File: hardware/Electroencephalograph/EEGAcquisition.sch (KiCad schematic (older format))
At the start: 59 parts, among them U1 ADS1298IPAG, U2 OPA330xxD

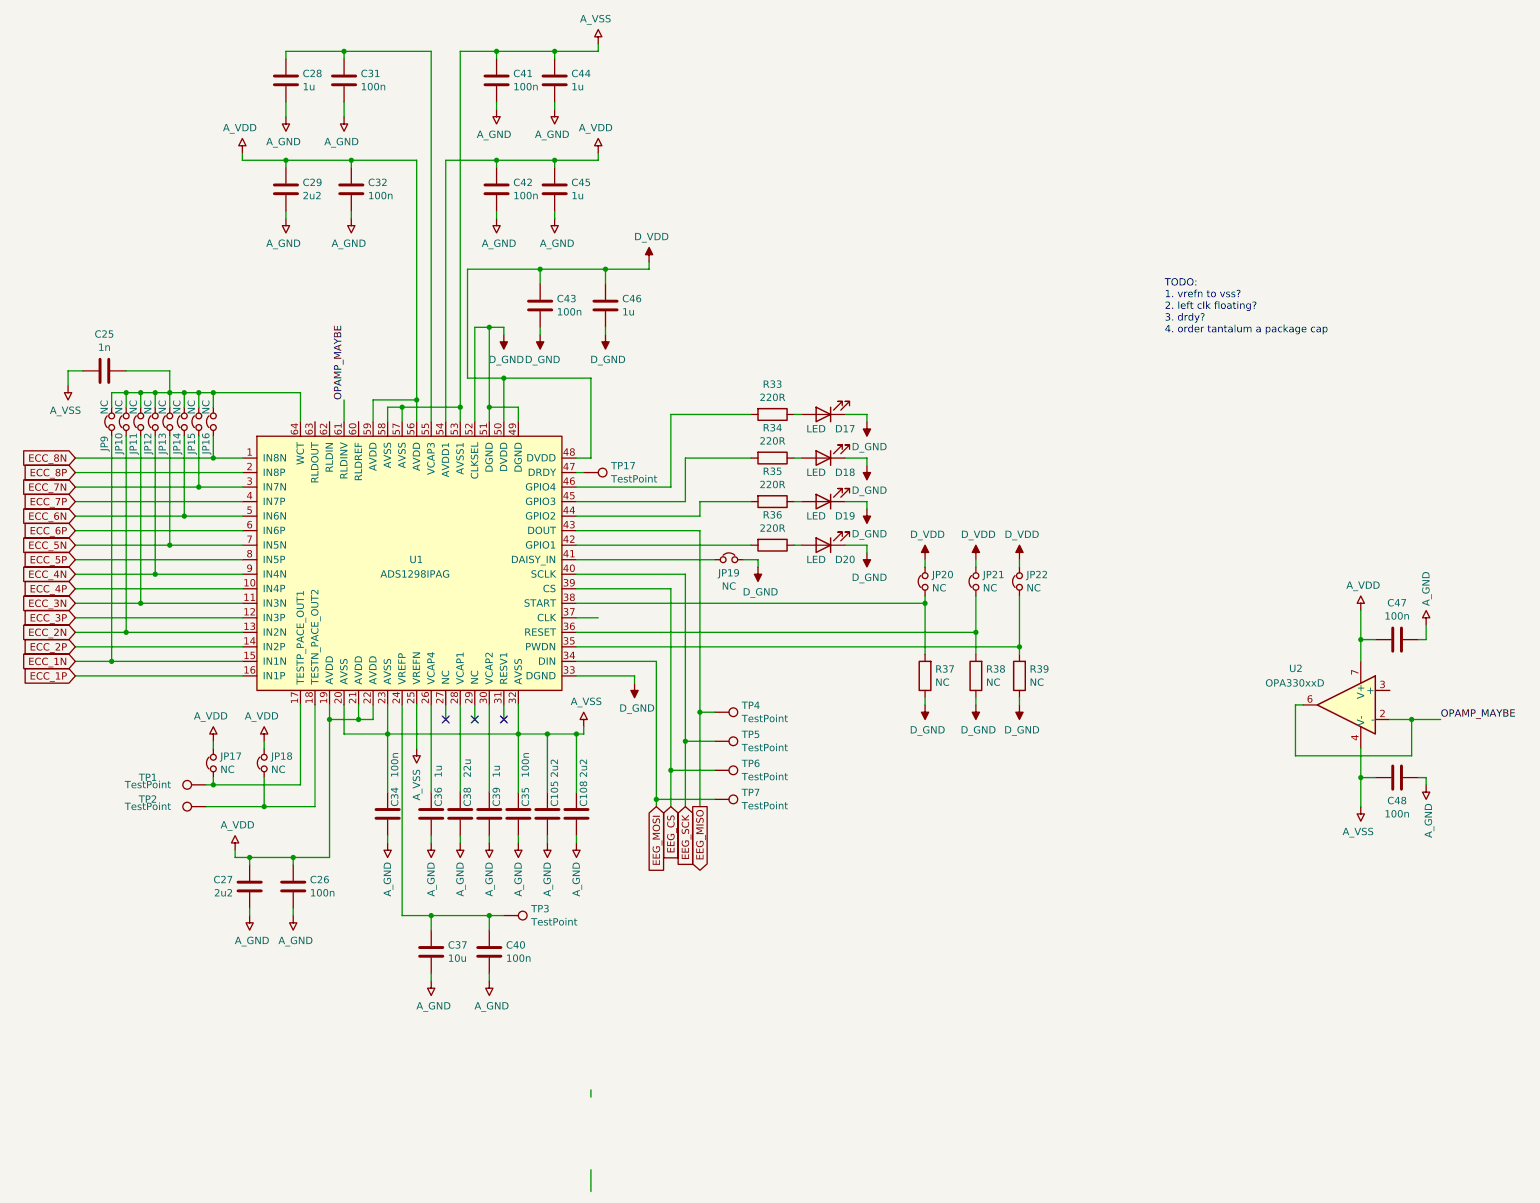
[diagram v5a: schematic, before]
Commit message: placement of usb interface, fix in grounds
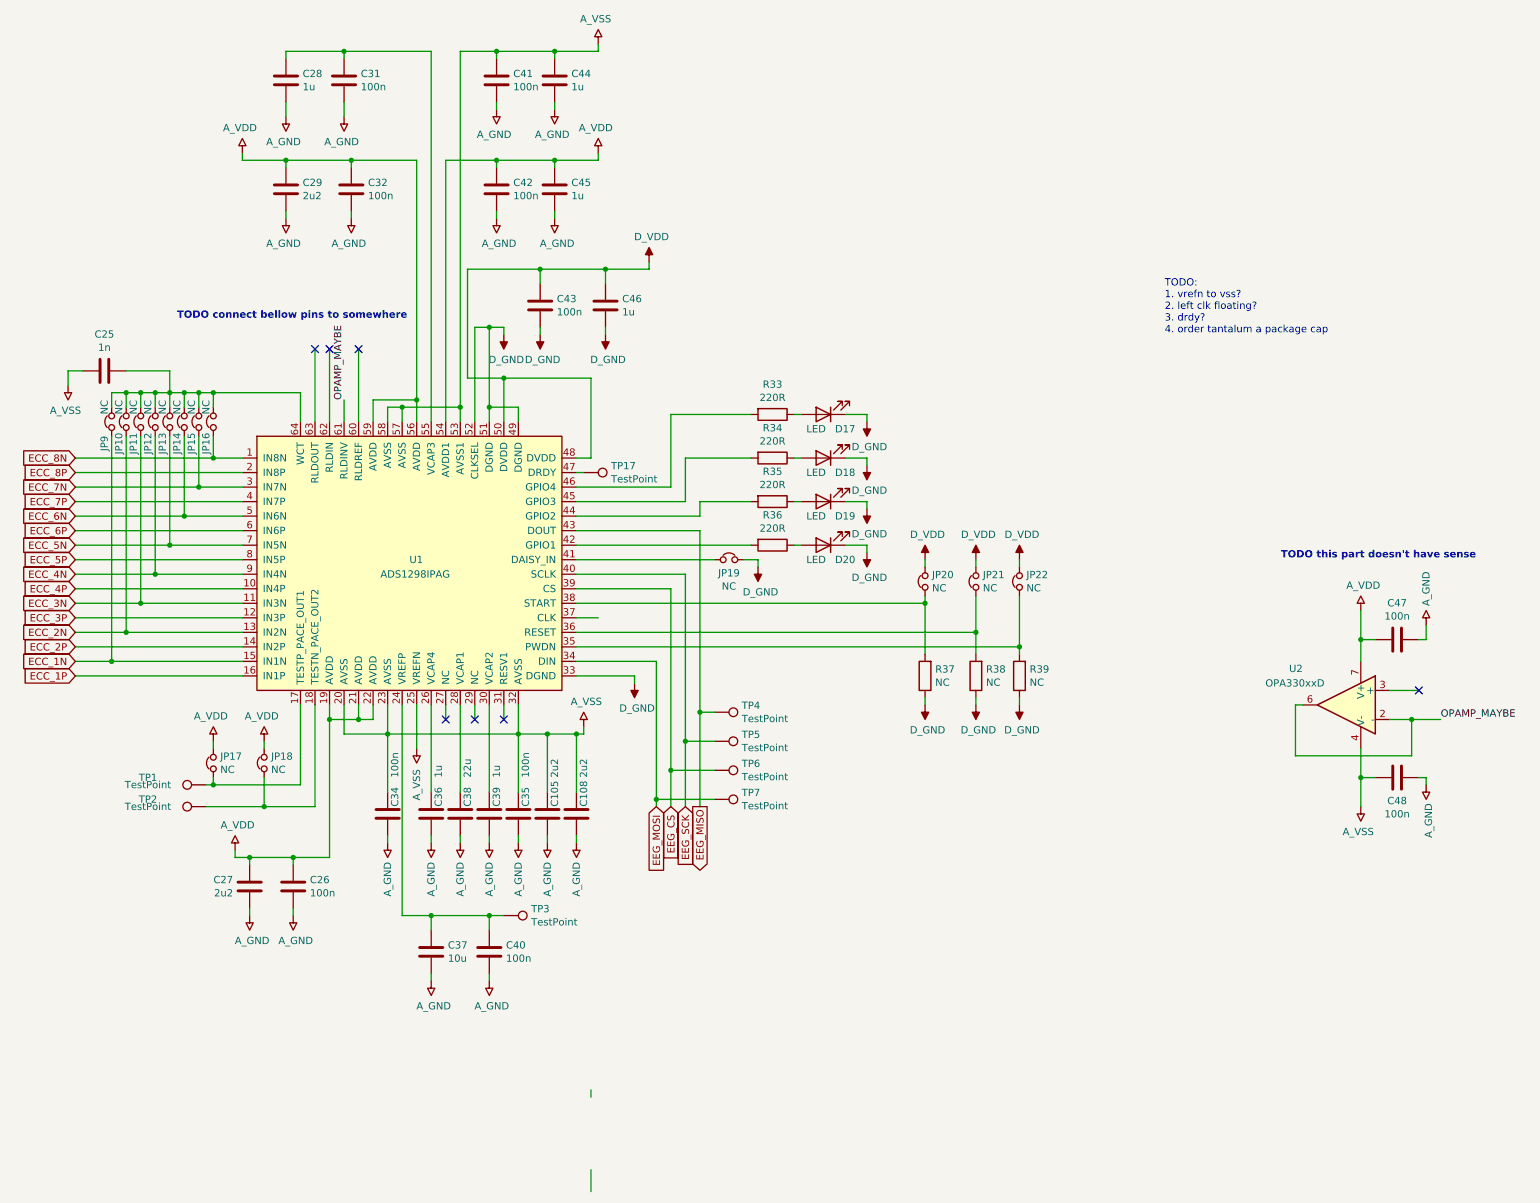
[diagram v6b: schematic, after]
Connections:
- no-connect marks 3 -> 7
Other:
- note added: "TODO connect bellow pins to somewhere"
- note added: "TODO this part doesn't have sense"
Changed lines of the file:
@@
 encoding utf-8
 Sheet 3 8
-Title ""
+Title "EEG analog to digital conversion"
 Date ""
-Rev ""
-Comp ""
+Rev "1.0"
+Comp "MIT License"
 Comment1 ""
 Comment2 ""
@@
 Wire Wire Line
 	2500 1550 2950 1550
+Wire Wire Line
+	2700 3350 2700 2850
+Wire Wire Line
+	2800 3350 2800 2850
+Wire Wire Line
+	3000 3350 3000 2850
+NoConn ~ 3000 2850
+NoConn ~ 2800 2850
+NoConn ~ 2700 2850
+Text Notes 1750 2650 0    50   ~ 10
+TODO connect bellow pins to somewhere
+Wire Wire Line
+	10100 5200 10300 5200
+NoConn ~ 10300 5200
+Text Notes 9350 4300 0    50   ~ 10
+TODO this part doesn't have sense
 $EndSCHEMATC

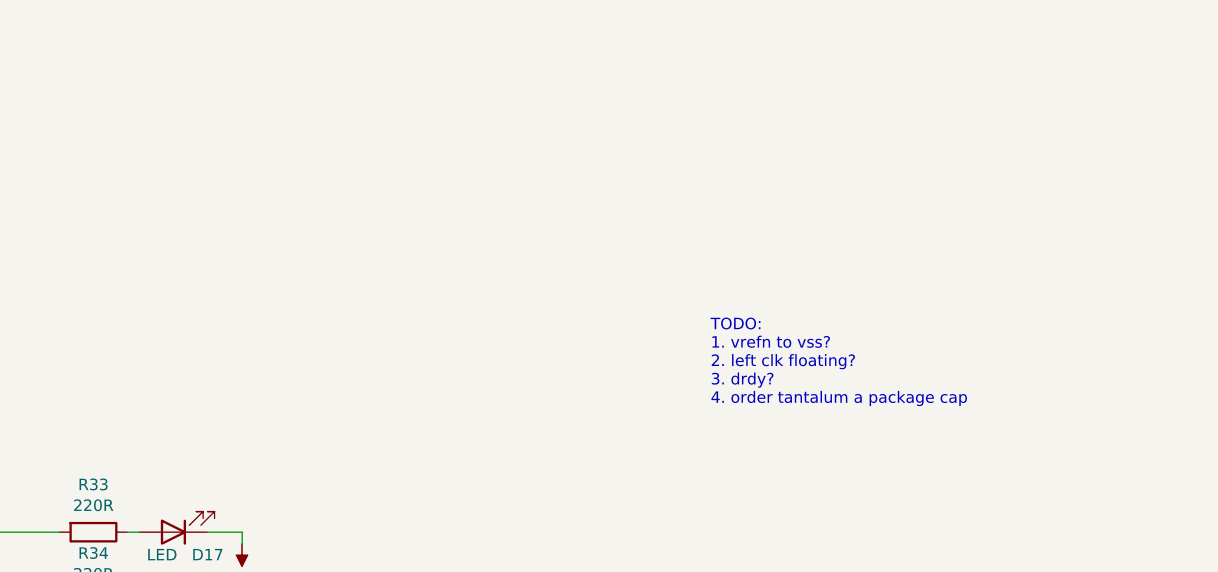
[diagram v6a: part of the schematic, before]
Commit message: fix #41, fix #18
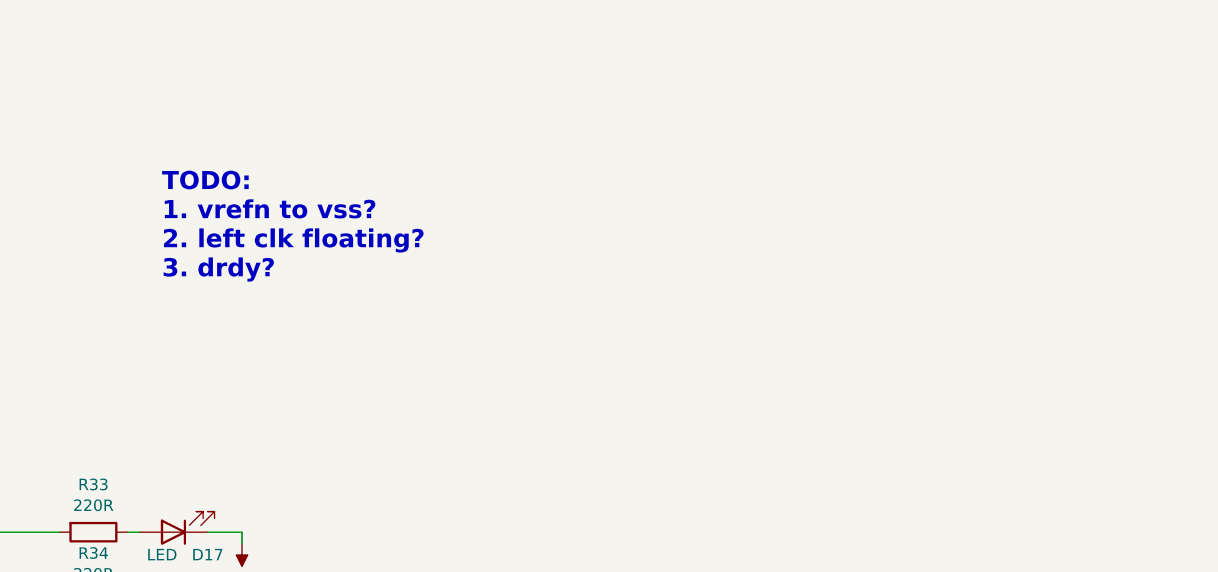
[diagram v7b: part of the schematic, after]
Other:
- note added: "TODO: \n1. vrefn to vss?\n2. left clk floating?\n3. drdy?"
- note removed: "TODO: \n1. vrefn to vss?\n2. left clk floating?\n3. drdy?\n4. order tantalum a package cap"
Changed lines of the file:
@@
 $Descr A4 11693 8268
 encoding utf-8
-Sheet 3 8
+Sheet 3 9
 Title "EEG analog to digital conversion"
 Date ""
@@
 Wire Wire Line
 	2350 5600 2350 5550
-Text Notes 8550 2750 0    50   ~ 0
-TODO: \n1. vrefn to vss?\n2. left clk floating?\n3. drdy?\n4. order tantalum a package cap
-$Comp
-L Device:C C?
+Text Notes 6150 2200 0    79   ~ 16
+TODO: \n1. vrefn to vss?\n2. left clk floating?\n3. drdy?
+$Comp
+L Device:C C?
